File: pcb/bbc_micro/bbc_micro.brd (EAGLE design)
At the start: 56 x 65 mm, 27 parts, among them IC1 STM32F072C8T6, SW1 324_SW, SW2 324_SW, SW3 324_SW

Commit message: working on bbc micro PCB
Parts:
- added U$9: GAMEPORT_15P, ibmpc:DA15
- JP3: device pinhead:2X04 -> pinhead:2X03
- moved JP2 50.3 mm to (21.0, 57.7), turned to 0 degrees
- moved R12 16.8 mm to (37.3, 54.4), turned to 0 degrees
- moved LED2 16.0 mm to (37.3, 52.5)
- moved R14 15.2 mm to (47.2, 63.2)
- moved R13 15.1 mm to (47.2, 59.4)
- moved J4 14.6 mm to (40.5, 57.2)
- moved LED3 12.1 mm to (37.3, 50.0)
- moved R15 12.1 mm to (37.3, 47.8)
- moved JP3 7.78 mm to (34.5, 42.8)
- moved C8 2.64 mm to (26.4, 43.9)
- moved JP4 2.02 mm to (48.8, 34.5)
- moved C7 1.44 mm to (26.3, 33.9), turned to 90 degrees
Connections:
- removed net N$27: IC1.38, JP3.1, R15.1
- removed net N$6: IC1.39, JP3.2, R12.1
- net +3V3: now also JP3.3; no longer JP3.5
- net GND: now also JP3.4; no longer JP3.6
- net N$12: now also JP3.5; no longer JP3.7
- net N$14: now also JP3.6; no longer JP3.8
- net N$15: now also JP3.1; no longer JP3.3
- net N$16: now also JP3.2; no longer JP3.4
- net N$8: now also R12.1
- net N$9: now also R15.1
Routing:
- net ROW_B: track 0.00 -> 42.4 mm, vias 0 -> 1
- net ROW_A: track 0.00 -> 36.5 mm, vias 0 -> 1
- net N$8: track 0.00 -> 33.8 mm
- net N$9: track 3.50 -> 32.9 mm
- net N$16: track 0.00 -> 12.9 mm
- net N$23: track 51.5 -> 61.6 mm
- net N$14: track 0.00 -> 9.94 mm
- net N$15: track 0.00 -> 8.67 mm
- net N$22: track 53.6 -> 61.8 mm
- net N$12: track 0.00 -> 7.19 mm
- net GND: track 5.79 -> 0.00 mm
- net N$37: track 23.7 -> 28.8 mm
- net N$18: track 25.9 -> 21.6 mm
- net +3V3: track 35.3 -> 33.0 mm
- net N$28: track 0.21 -> 2.30 mm
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
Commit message: almost done with pcb
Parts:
- added C1: 100nF, clock:0805@1
- added R1, R16, R17, R18, R19, R2, R3, R4, R5, R6, R8: 5.1K, SparkFun-Passives:0805
- added R10: 2K, SparkFun-Passives:0805
- added U$5: MCP4451, ps2:TSSOP20
- U$9: value GAMEPORT_15P -> BBC_15P; device ibmpc:DA15 -> bbc_micro:DA15
- moved SW1 3.67 mm to (11.3, 36.8)
- moved SW2 3.54 mm to (11.3, 41.7)
- moved R11 3.49 mm to (11.6, 44.6)
- moved R9 3.36 mm to (11.6, 34.0)
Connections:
- new net N$10: U$5.19, U$9.12
- new net N$11: U$5.12, U$9.4
- new net N$17: U$5.10, U$5.3, U$9.14
- new net N$19: U$5.11, U$5.18, U$9.11
- new net N$20: R18.1, R19.1, U$9.1
- new net N$21: R18.2, U$9.10
- new net N$24: R19.2, U$9.13
- new net N$4: R10.1, U$5.4
- new net N$5: U$5.2, U$9.7
- new net N$6: U$5.9, U$9.15
- net +3V3: now also C1.2, R16.2, R17.2, U$5.17
- net /EN: now also IC1.20
- net BREAK: now also IC1.19
- net CA2: now also IC1.28
- net CB1/XA: now also IC1.4, R1.1
- net CB2/YA: now also IC1.3, R2.1
- net D0/XD: now also IC1.2, R3.1
- net D2/YD: now also IC1.41, R4.1
- net D5/LEFT: now also IC1.40, R5.1
- net D6/MIDDLE: now also IC1.39, R6.1
- net D7/RIGHTT: now also IC1.38, R8.1
- net GND: now also C1.1, R10.2, U$5.16, U$5.7, U$9.2, U$9.3, U$9.5, U$9.6, U$9.8, U$9.G1, U$9.G2
- net N$22: now also R16.1, U$5.5
- net N$23: now also R17.1, U$5.6
- net N$37: now also IC1.6; no longer IC1.2
- net USER_PORT_5V: now also R1.2, R2.2, R3.2, R4.2, R5.2, R6.2, R8.2
- net W: now also IC1.29
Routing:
- net +5V: track 9.56 -> 131.7 mm, vias 0 -> 3
- net USER_PORT_5V: track 0.00 -> 64.3 mm, vias 0 -> 1
- net BREAK: track 0.00 -> 35.7 mm
- net /EN: track 0.00 -> 30.3 mm
- net CA2: track 0.00 -> 25.5 mm
- net CB1/XA: track 0.00 -> 24.8 mm, vias 0 -> 1
- net N$20: track 0.00 -> 24.6 mm, vias 0 -> 1
- net N$19: track 0.00 -> 23.0 mm
- net CB2/YA: track 0.00 -> 22.7 mm, vias 0 -> 1
- net N$10: track 0.00 -> 21.7 mm
- net D0/XD: track 0.00 -> 21.4 mm, vias 0 -> 1
- net N$17: track 0.00 -> 20.1 mm
- net N$23: track 61.6 -> 80.7 mm
- net N$22: track 61.8 -> 79.8 mm
- net W: track 0.00 -> 17.5 mm
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
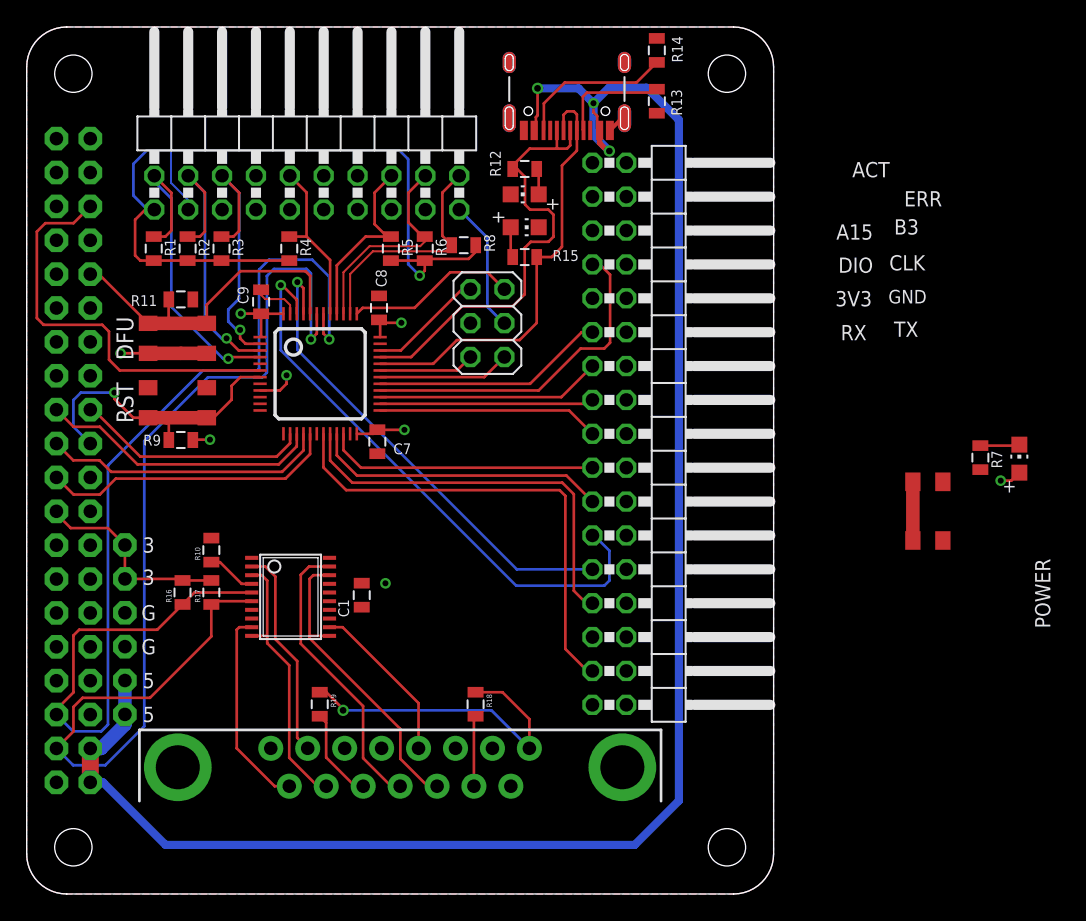
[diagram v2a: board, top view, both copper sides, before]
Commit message: hooked up digital pot and leds
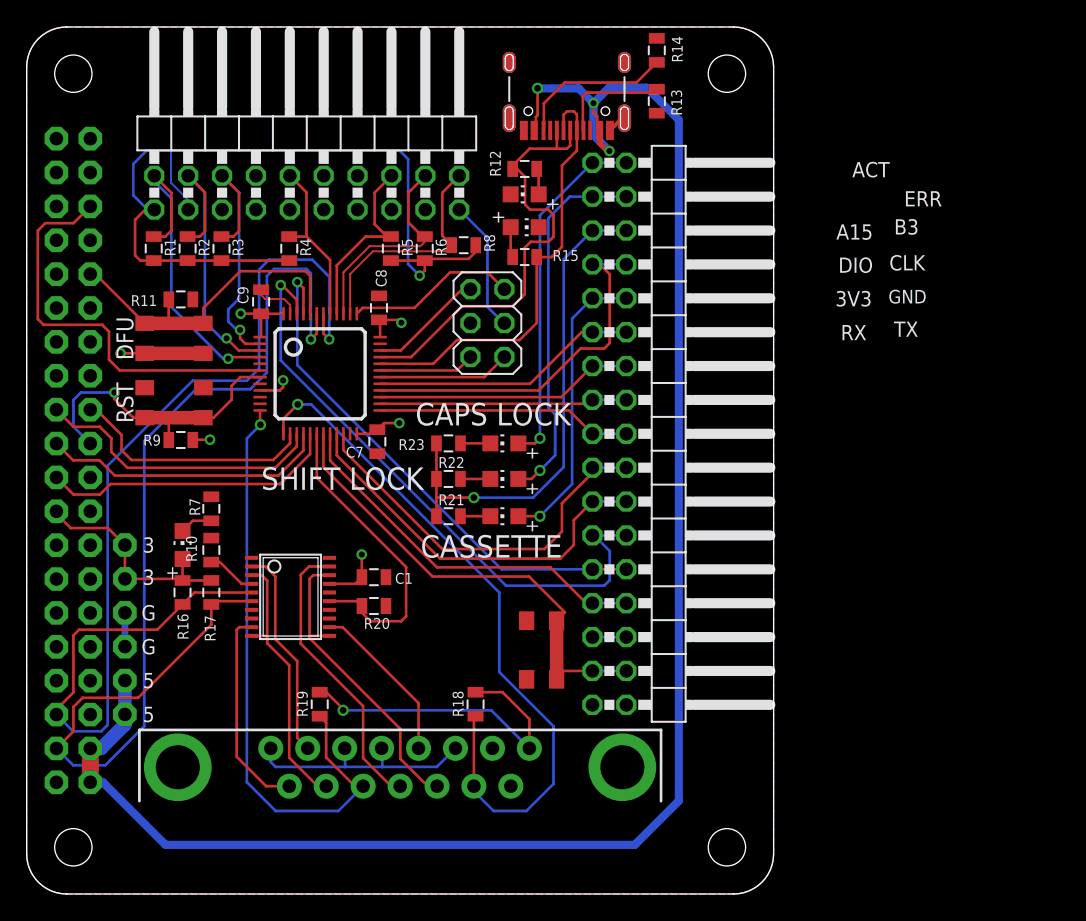
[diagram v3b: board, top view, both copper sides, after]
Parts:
- added LED4, LED5, LED6: (no value), adafruit:CHIP-LED0805
- added R20: 5.1K, SparkFun-Passives:0805
- added R21, R22, R23: 2K, SparkFun-Passives:0805
- moved LED1 63.1 mm to (11.7, 26.2)
- moved R7 57.8 mm to (13.8, 28.9), turned to 270 degrees
- moved SW3 30.8 mm to (38.6, 18.3), turned to 270 degrees
- moved C1 1.63 mm to (26.0, 23.7), turned to 180 degrees
- moved SW1 0.25 mm to (11.0, 36.8)
- moved SW2 0.25 mm to (11.0, 41.7)
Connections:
- removed net N$24: R19.2, U$9.13
- new net N$25: IC1.18, R20.1, U$5.15
- new net N$26: LED5.C, R22.2
- new net N$27: LED6.C, R23.2
- new net N$30: IC1.12, R19.2, U$9.13
- net BREAK: now also SW3.P$2, SW3.P$3
- net GND: now also R20.2
- net KB_5V: now also R21.1, R22.1, R23.1
- net LED_CAPSLOCK: now also LED6.A
- net LED_CASSETTE: now also LED4.A
- net LED_SHIFTLOCK: now also LED5.A
- net N$21: now also IC1.13
- net N$3: now also LED4.C, R21.2; no longer SW3.P$2, SW3.P$3
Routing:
- net N$21: track 5.30 -> 52.7 mm, vias 0 -> 1
- net N$30: track 0.00 -> 45.6 mm, vias 0 -> 1
- net KB_5V: track 0.00 -> 37.1 mm, vias 0 -> 1
- net LED_SHIFTLOCK: track 0.00 -> 28.0 mm, vias 0 -> 1
- net LED_CAPSLOCK: track 0.00 -> 26.6 mm, vias 0 -> 1
- net N$25: track 0.00 -> 23.3 mm
- net LED_CASSETTE: track 0.00 -> 22.1 mm, vias 0 -> 1
- net GND: track 14.9 -> 35.9 mm
- net COL_A: track 20.4 -> 29.5 mm
- net ROW_C: track 22.2 -> 29.4 mm
- net N$24: track 6.96 -> 0.00 mm
- net +3V3: track 39.4 -> 42.8 mm, vias 8 -> 7
- net ROW_A: track 36.6 -> 39.8 mm
- net ROW_B: track 43.7 -> 46.7 mm
- net W: track 17.5 -> 20.1 mm
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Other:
- board text added: "CAPS LOCK"
- board text added: "CASSETTE"
- board text added: "SHIFT LOCK"
- board text removed: "POWER"

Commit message: bbc micro protocol board test board
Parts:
- added U$1: PINHD1X2, adafruit_changed:1X02
- moved R7 0.92 mm to (14.7, 28.4), turned to 180 degrees
- moved LED1 0.76 mm to (11.7, 26.9)
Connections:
- new net N$24: IC1.10, U$1.1
- new net N$31: IC1.11, U$1.2
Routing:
- net +3V3: track 42.8 -> 57.3 mm
- net N$31: track 0.00 -> 3.92 mm
- net N$13: track 22.7 -> 26.2 mm
- net N$24: track 0.00 -> 2.25 mm
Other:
- board text added: "BREAK"
- board text added: "PT0 dekuNukem AUG2022"
- board text added: "USB4VC Protocol Card for BBC Micro"
- board text removed: "A15"
- board text removed: "ACT"
- board text removed: "B3"
- board text removed: "ERR"
- board text removed: "PT3 dekuNukem JUL2022"
- board text removed: "USB4VC Protocol Card for Apple Lisa, Early Macintosh & Apple Desktop Bus"
